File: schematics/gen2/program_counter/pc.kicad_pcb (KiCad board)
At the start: 2 copper layers, 96.5 x 92 mm, 16 parts, among them U10 74LS193, U11 74LS193, U12 74LS193, U13 74LS245, U14 74LS245, U8 74LS00, U9 74LS193

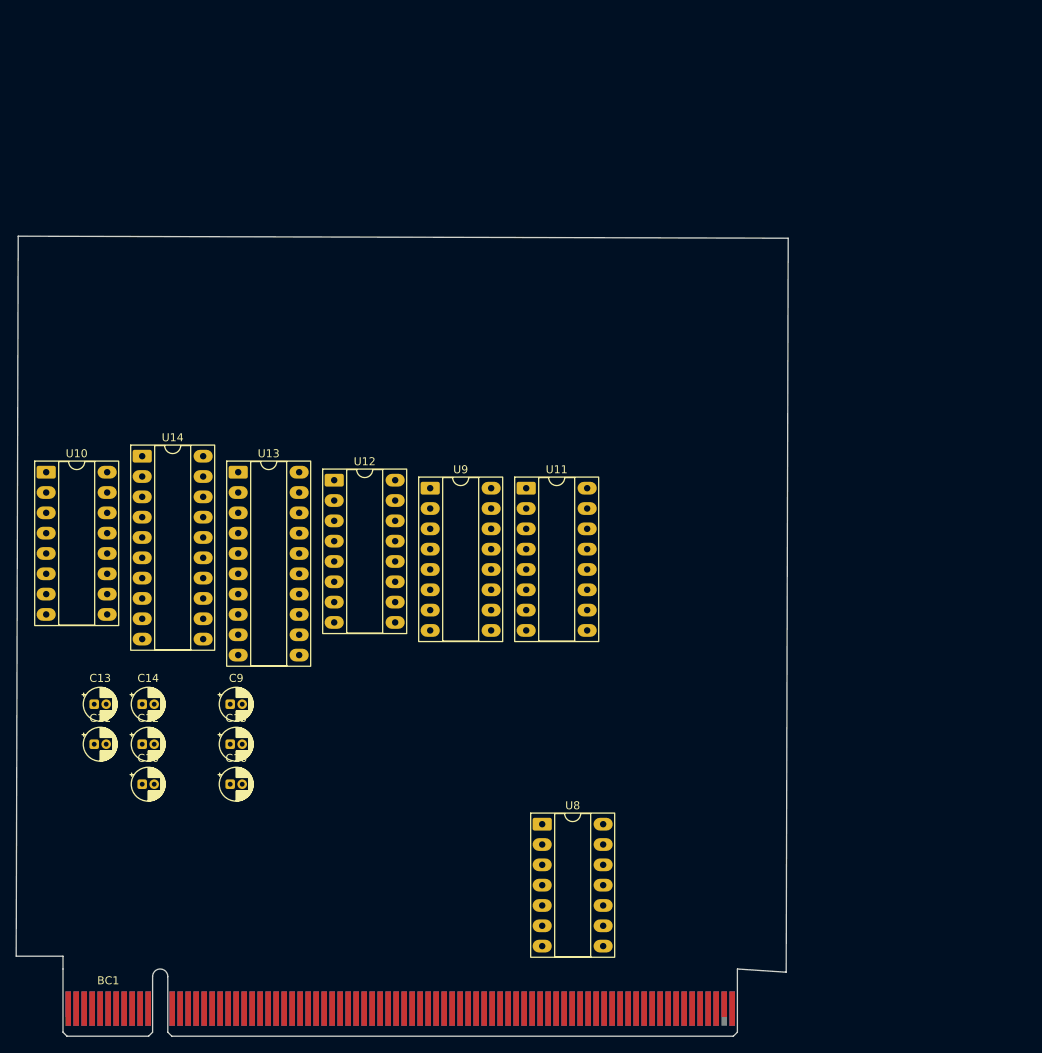
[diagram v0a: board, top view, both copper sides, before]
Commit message: (feat) stack pointer and program counter pcb, QA needed.
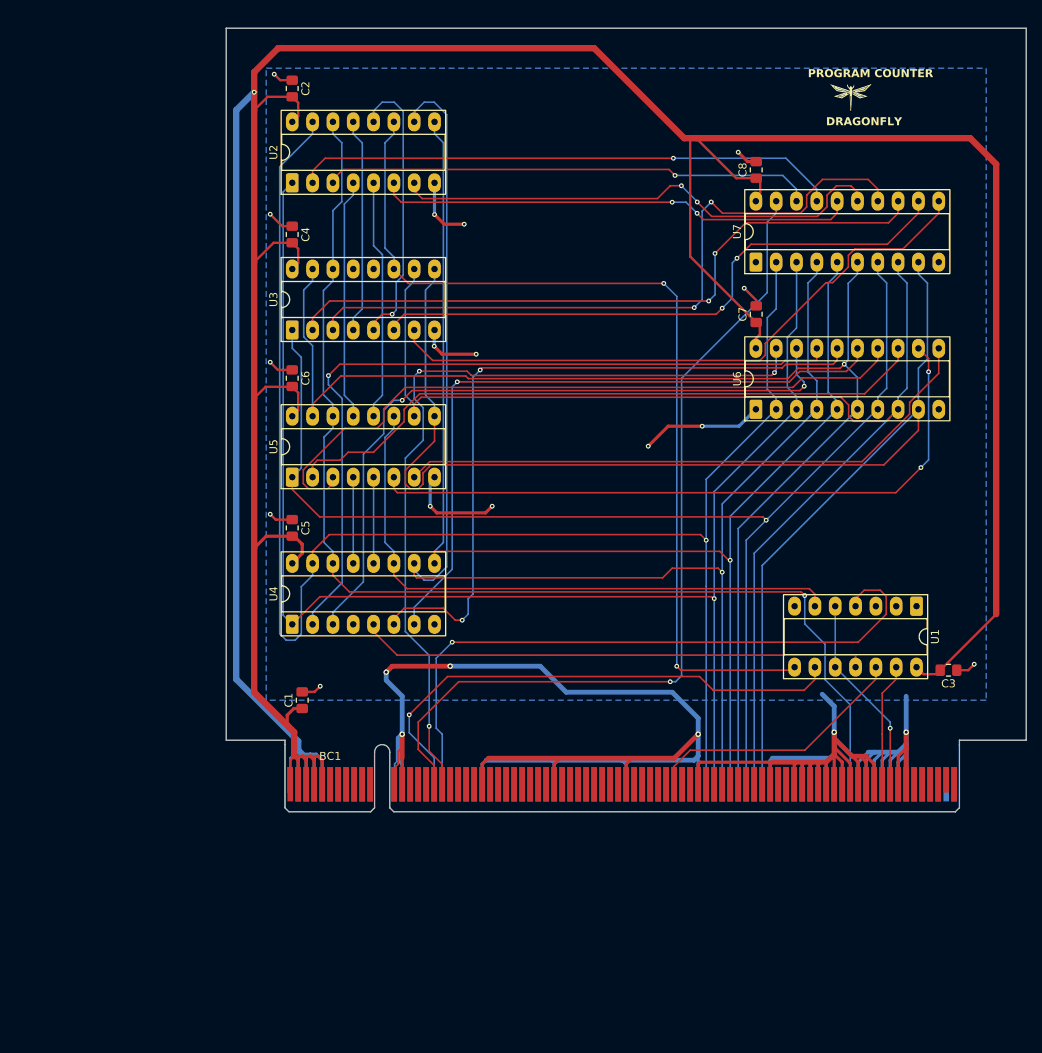
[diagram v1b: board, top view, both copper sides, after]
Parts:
- removed C10, C11, C12, C13, C14, C15, C16, C9: C, Capacitor_THT:CP_Radial_D4.0mm_P1.50mm
- removed U10, U11, U12, U9: 74LS193, Package_DIP:DIP-16_W7.62mm_Socket_LongPads
- removed U13, U14: 74LS245, Package_DIP:DIP-20_W7.62mm_Socket_LongPads
- removed U8: 74LS00, Package_DIP:DIP-14_W7.62mm_Socket_LongPads
- added C1: C, Capacitor_SMD:C_0805_2012Metric_Pad1.18x1.45mm_HandSolder, F.Cu at (116.0, 119.5)
- added C2: C, Capacitor_SMD:C_0805_2012Metric_Pad1.18x1.45mm_HandSolder, F.Cu at (114.8, 43.0)
- added C3: C, Capacitor_SMD:C_0805_2012Metric_Pad1.18x1.45mm_HandSolder, F.Cu at (196.8, 115.8)
- added C4: C, Capacitor_SMD:C_0805_2012Metric_Pad1.18x1.45mm_HandSolder, F.Cu at (114.8, 61.3)
- added C5: C, Capacitor_SMD:C_0805_2012Metric_Pad1.18x1.45mm_HandSolder, F.Cu at (114.8, 98.0)
- added C6: C, Capacitor_SMD:C_0805_2012Metric_Pad1.18x1.45mm_HandSolder, F.Cu at (114.8, 79.2)
- added C7: C, Capacitor_SMD:C_0805_2012Metric_Pad1.18x1.45mm_HandSolder, F.Cu at (172.8, 71.2)
- added C8: C, Capacitor_SMD:C_0805_2012Metric_Pad1.18x1.45mm_HandSolder, F.Cu at (172.8, 53.2)
- added U1: 74HC00, Package_DIP:DIP-14_W7.62mm_Socket_LongPads, F.Cu at (192.8, 107.8)
- added U2: 74HC193, Package_DIP:DIP-16_W7.62mm_Socket_LongPads, F.Cu at (114.8, 54.8)
- added U3: 74HC193, Package_DIP:DIP-16_W7.62mm_Socket_LongPads, F.Cu at (114.8, 73.2)
- added U4: 74HC193, Package_DIP:DIP-16_W7.62mm_Socket_LongPads, F.Cu at (114.8, 110.0)
- added U5: 74HC193, Package_DIP:DIP-16_W7.62mm_Socket_LongPads, F.Cu at (114.8, 91.6)
- added U6: 74HC245, Package_DIP:DIP-20_W7.62mm_Socket_LongPads, F.Cu at (172.7, 83.1)
- added U7: 74HC245, Package_DIP:DIP-20_W7.62mm_Socket_LongPads, F.Cu at (172.7, 64.7)
- moved BC1 39.5 mm to (114.5, 130.0)
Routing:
- net VCC: track 0.00 -> 473.6 mm, vias 0 -> 1
- net GND: track 0.00 -> 378.4 mm, vias 0 -> 22
- net /DATA0: track 0.00 -> 200.1 mm, vias 0 -> 1
- net /DATA2: track 0.00 -> 182.1 mm, vias 0 -> 1
- net /DATA1: track 0.00 -> 180.8 mm, vias 0 -> 1
- net /DATA7: track 0.00 -> 174.5 mm
- net /DATA3: track 0.00 -> 167.9 mm, vias 0 -> 1
- net /DATA4: track 0.00 -> 163.6 mm, vias 0 -> 1
- net /DATA6: track 0.00 -> 158.0 mm
- net /DATA5: track 0.00 -> 154.7 mm, vias 0 -> 1
- net /RESET: track 0.00 -> 145.5 mm, vias 0 -> 1
- net /Ph: track 0.00 -> 117.4 mm, vias 0 -> 2
- net /~{RPCH}: track 0.00 -> 108.1 mm, vias 0 -> 1
- net /~{RPCL}: track 0.00 -> 103.1 mm, vias 0 -> 3
- net /DL1: track 0.00 -> 96.7 mm, vias 0 -> 1
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- added copper zone on B.Cu, net GND
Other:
- board size 96.5 x 92 mm -> 100 x 89.5 mm
- board text added: "DRAGONFLY"
- board text added: "PROGRAM COUNTER"

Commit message: program counter complete
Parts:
- added R1: R, Resistor_THT:R_Axial_DIN0207_L6.3mm_D2.5mm_P7.62mm_Horizontal, F.Cu at (200.0, 119.9)
- C1: footprint Capacitor_SMD:C_0805_2012Metric_Pad1.18x1.45mm_HandSolder -> Capacitor_THT:C_Radial_D6.3mm_H5.0mm_P2.50mm
- C2, C3, C4, C5, C6, C7, C8: footprint Capacitor_SMD:C_0805_2012Metric_Pad1.18x1.45mm_HandSolder -> Capacitor_THT:C_Disc_D3.0mm_W1.6mm_P2.50mm
- moved U5 66.1 mm to (176.5, 67.8)
- moved U3 65.3 mm to (176.5, 51.8)
- moved C6 58.0 mm to (169.5, 60.0), turned to 0 degrees
- moved C4 57.4 mm to (169.5, 44.0), turned to 0 degrees
- moved U4 45.1 mm to (130.6, 67.8)
- moved C5 39.1 mm to (124.0, 60.0), turned to 0 degrees
- moved C8 38.8 mm to (155.5, 88.0), turned to 180 degrees
- moved C7 37.5 mm to (155.5, 104.5), turned to 180 degrees
- moved U7 33.6 mm to (160.0, 95.9)
- moved U6 31.6 mm to (160.0, 112.1)
- moved U2 16.1 mm to (130.6, 51.8)
- moved C2 9.30 mm to (124.0, 44.0), turned to 0 degrees
- moved U1 7.37 mm to (200.1, 108.5), turned to 180 degrees
- moved C3 4.54 mm to (192.5, 114.2), turned to 90 degrees
- moved C1 1.82 mm to (116.5, 117.8), turned to 0 degrees
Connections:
- U1 pad 1: unconnected-(U1-Pad1) -> Net-(R1-Pad2)
- U1 pad 2: unconnected-(U1-Pad2) -> Net-(R1-Pad2)
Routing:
- net VCC: track 473.6 -> 61.4 mm
- net GND: track 378.4 -> 127.8 mm, vias 22 -> 9
- net /Pl: track 75.9 -> 162.2 mm, vias 0 -> 2
- net /DATA0: track 200.1 -> 114.7 mm, vias 1 -> 2
- net /DATA2: track 182.1 -> 98.1 mm, vias 1 -> 0
- net /DATA7: track 174.5 -> 96.2 mm
- net /RESET: track 145.5 -> 218.4 mm, vias 1 -> 2
- net /DATA5: track 154.7 -> 82.2 mm, vias 1 -> 0
- net /DATA4: track 163.6 -> 92.2 mm, vias 1 -> 2
- net /DATA1: track 180.8 -> 109.9 mm, vias 1 -> 0
- net /DATA3: track 167.9 -> 98.1 mm, vias 1 -> 0
- net Net-(U2-~{BO}): track 27.0 -> 89.9 mm, vias 0 -> 2
- net /DATA6: track 158.0 -> 95.7 mm
- net /~{RPCL}: track 103.1 -> 44.1 mm, vias 3 -> 0
- net /~{RPCH}: track 108.1 -> 54.2 mm
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- added copper zone on F.Cu, net VCC
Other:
- board size 100 x 89.5 mm -> 100 x 91 mm
- board text added: "STACK POINTER"
- board text removed: "PROGRAM COUNTER"

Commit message: design + fix core_2
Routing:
- net /DH6: vias 0 -> 2
- net /DH7: vias 0 -> 2
- net /Ph: vias 0 -> 2
- net /Pl: vias 2 -> 4
- net /DL6: vias 0 -> 2
- net /DL4: vias 0 -> 2
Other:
- board text added: "PROGRAM COUNTER"
- board text removed: "DRAGONFLY"
- board text removed: "STACK POINTER"

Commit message: update core_2
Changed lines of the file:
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@@
 		(start 188.5 130)
 		(end 188.5 126)
-		(width 0.3)
+		(width 0.4)
 		(layer "F.Cu")
 		(net 106)
@@
 		(start 196.3 109.76)
 		(end 192.5 105.96)
-		(width 0.3)
+		(width 0.4)
 		(layer "F.Cu")
 		(net 106)
@@
 		(start 196.3 118.2)
 		(end 196.3 109.76)
-		(width 0.3)
+		(width 0.4)
 		(layer "F.Cu")
 		(net 106)
@@
 		(start 188.5 126)
 		(end 196.3 118.2)
-		(width 0.3)
+		(width 0.4)
 		(layer "F.Cu")
 		(net 106)

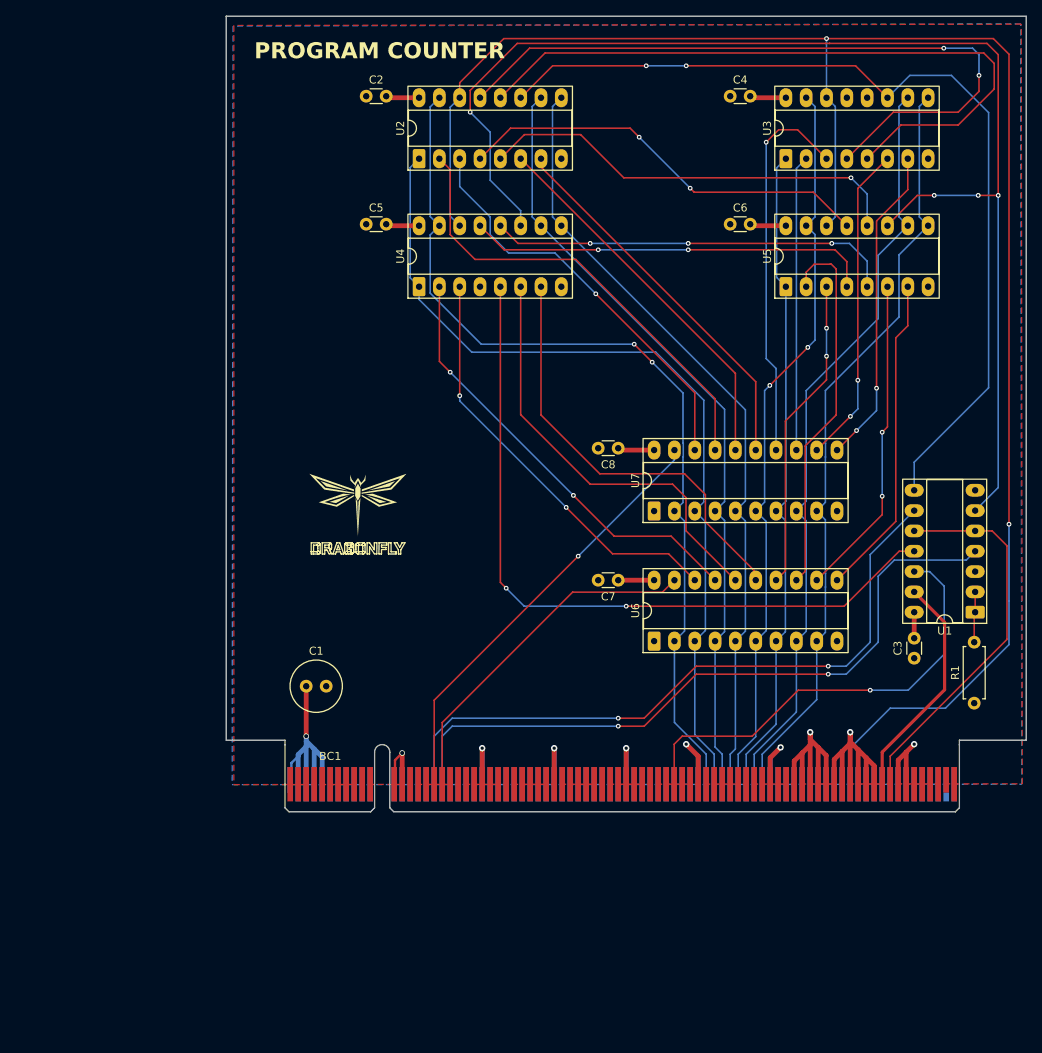
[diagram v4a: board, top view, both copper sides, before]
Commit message: fix(pc): changed resistor, capacitors footprints
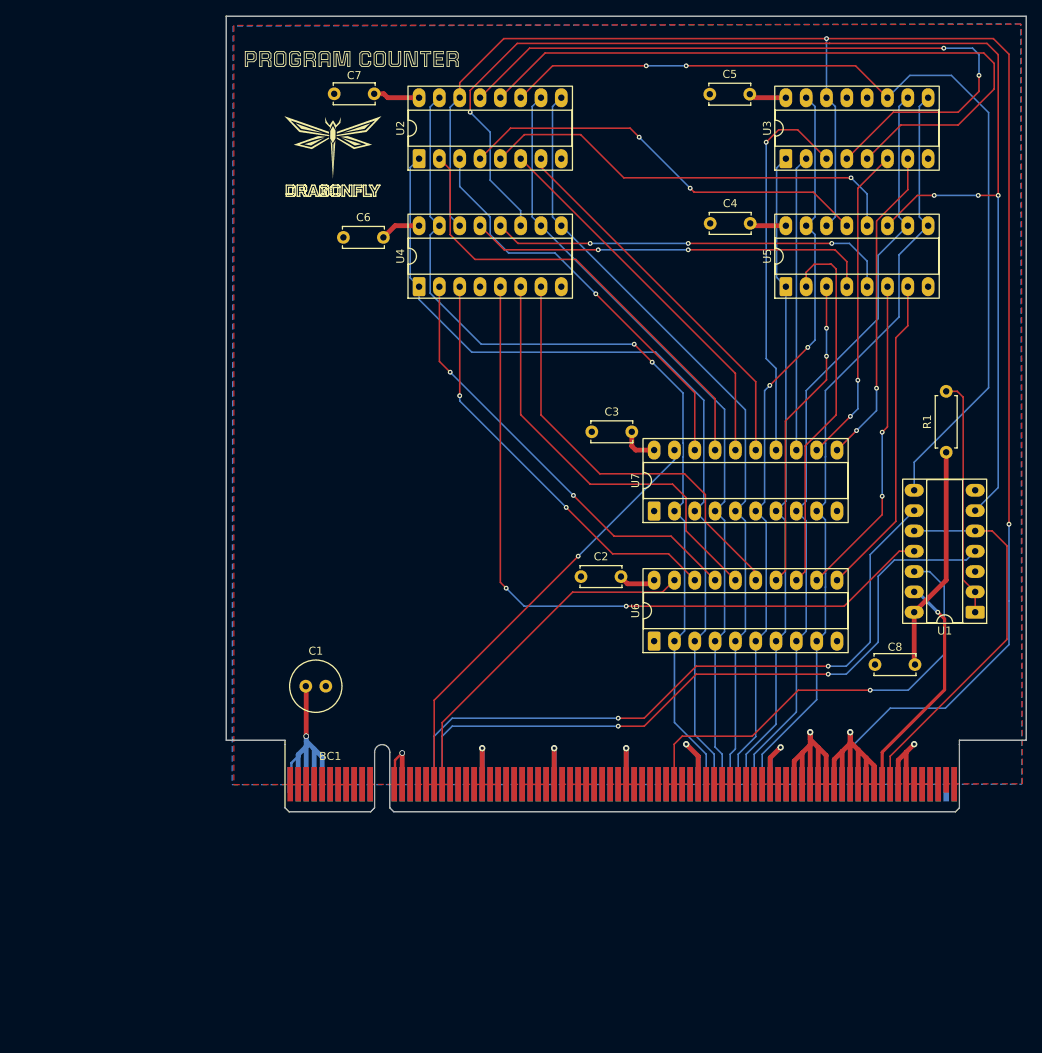
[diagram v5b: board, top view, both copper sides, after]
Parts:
- added kibuzzard-6911BE41: G***, kibuzzard-6911BE41, F.Cu at (122.2, 39.4)
- C2, C3, C4, C5, C6, C7, C8: footprint Capacitor_THT:C_Disc_D3.0mm_W1.6mm_P2.50mm -> Capacitor_THT:C_Disc_D5.0mm_W2.5mm_P5.00mm
- moved C7 68.0 mm to (125.0, 43.7)
- moved C2 65.8 mm to (150.8, 104.0)
- moved C3 49.2 mm to (152.2, 86.0), turned to 0 degrees
- moved C6 48.4 mm to (121.2, 61.6)
- moved C5 45.9 mm to (166.9, 43.8)
- moved C8 45.9 mm to (192.6, 115.0)
- moved R1 31.6 mm to (196.5, 88.5)
- moved C4 16.1 mm to (167.0, 59.9)
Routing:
- net VCC: track 61.4 -> 89.5 mm
- net Net-(R1-Pad2): track 6.45 -> 30.1 mm
- net /~{CLK}: track 28.8 -> 29.1 mm, vias 0 -> 1
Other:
- board text removed: "PROGRAM COUNTER"

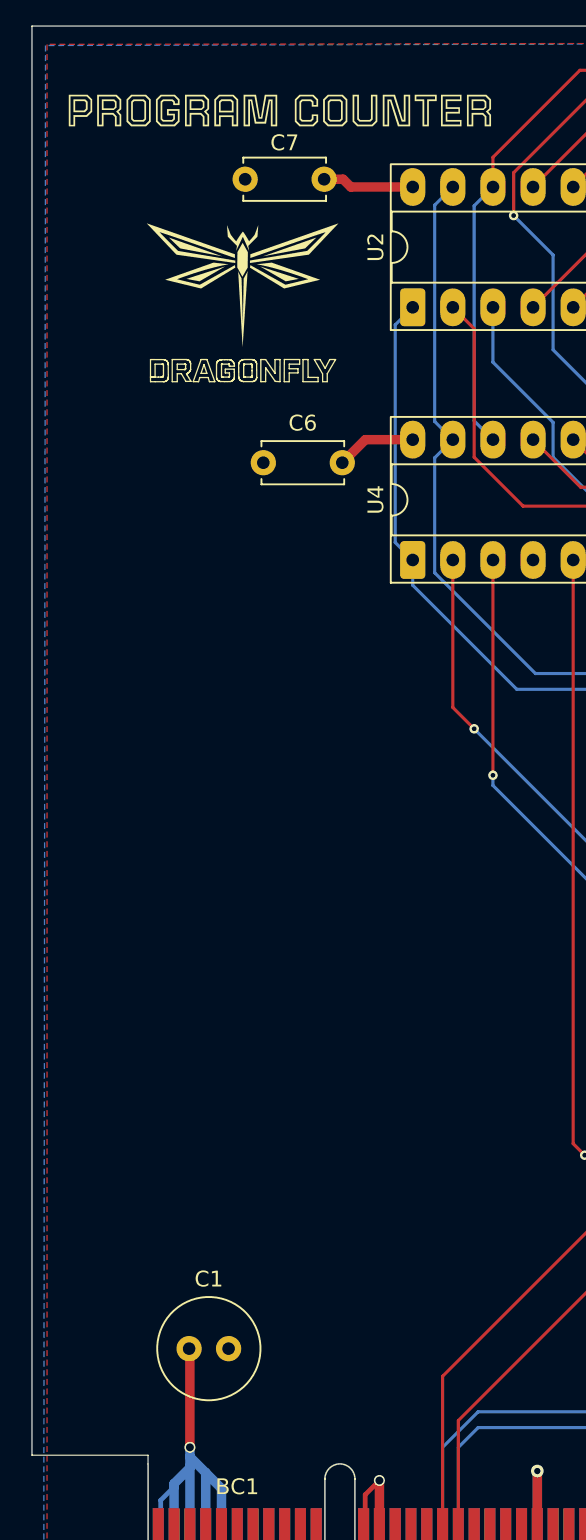
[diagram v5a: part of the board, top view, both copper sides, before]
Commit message: chore(kicad-pcb): added apps ucu logo
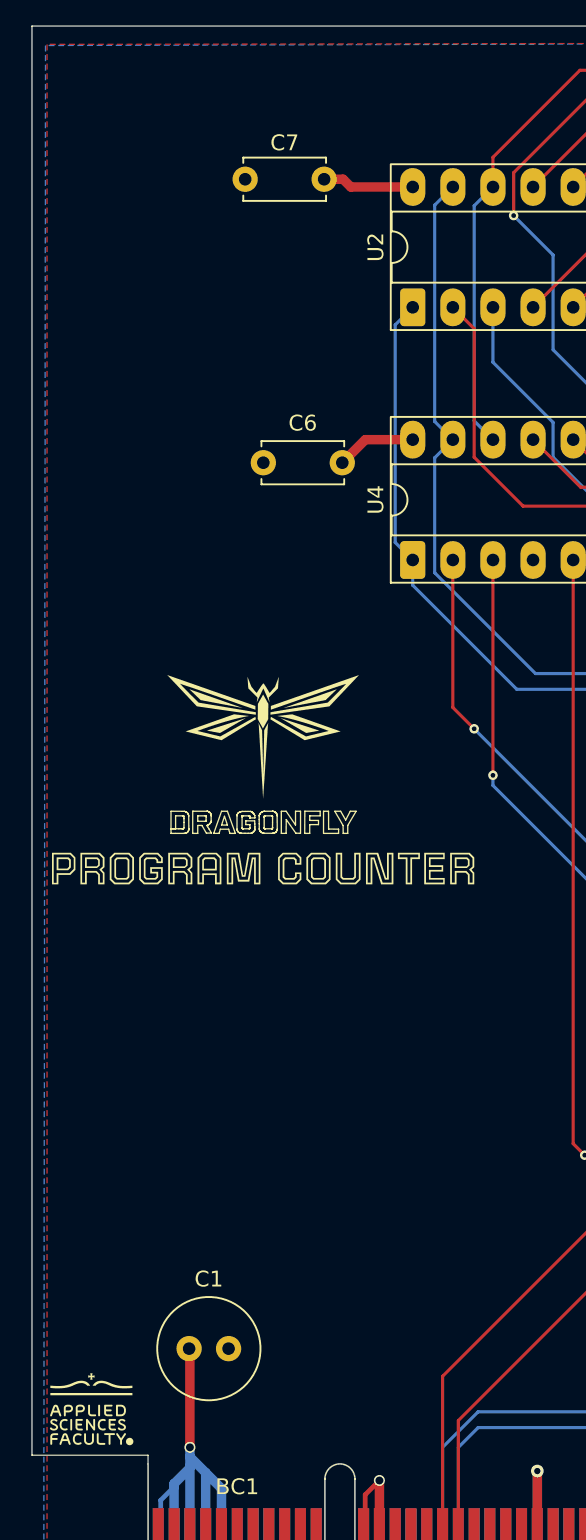
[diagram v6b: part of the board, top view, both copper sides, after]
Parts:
- moved kibuzzard-6911BE41 48.0 mm to (121.1, 87.3)
